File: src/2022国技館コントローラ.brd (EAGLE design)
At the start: 44 parts

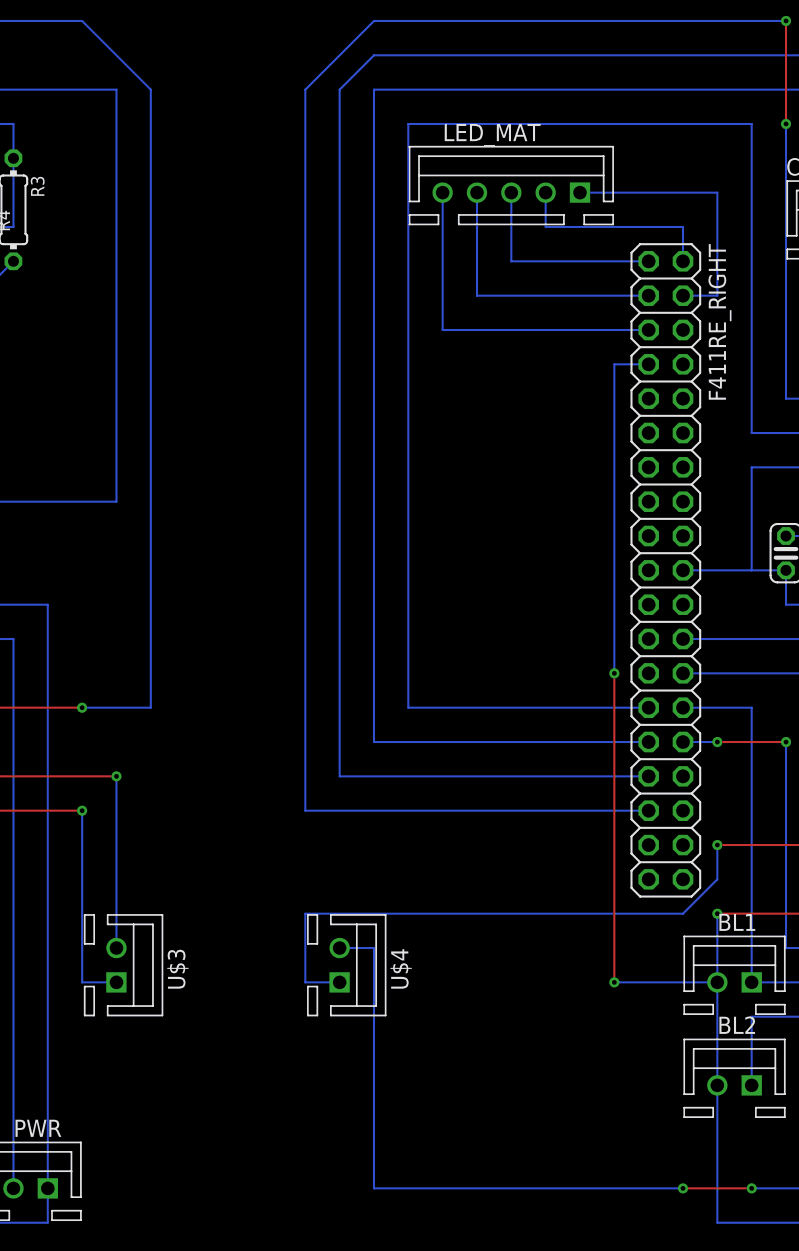
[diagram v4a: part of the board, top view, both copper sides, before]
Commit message: 足回りコントローラ
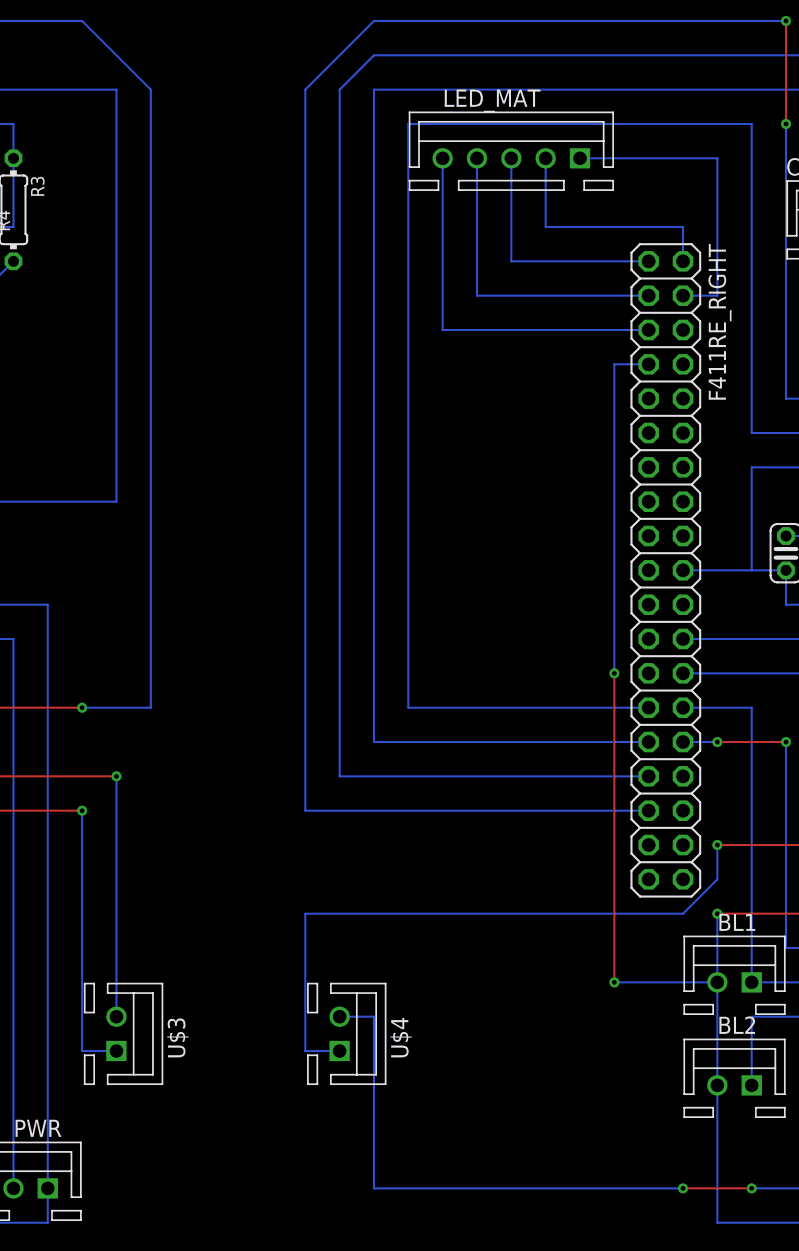
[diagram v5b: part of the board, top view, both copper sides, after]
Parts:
- moved U$3 5.08 mm to (57.1, 16.5)
- moved U$4 5.08 mm to (73.7, 16.5)
- moved LED_MAT 2.54 mm to (86.4, 81.3)
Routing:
- net U/D2: track 84.9 -> 95.0 mm
- net LED5: track 20.3 -> 22.9 mm
- net LED4: track 15.2 -> 17.8 mm
- net LED3: track 15.2 -> 17.8 mm
- net LED2: track 20.3 -> 22.9 mm
- net LED1: track 25.4 -> 27.9 mm
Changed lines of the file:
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@@
 <attribute name="VALUE" x="29.21" y="21.59" size="1.778" layer="27" ratio="10"/>
 </element>
-<element name="LED_MAT" library="con-jst-xh (1)" package="B5B-XH" value="" x="86.36" y="78.74" smashed="yes">
-<attribute name="NAME" x="81.28" y="82.55" size="1.27" layer="25"/>
-<attribute name="VALUE" x="81.28" y="74.93" size="1.27" layer="27"/>
+<element name="LED_MAT" library="con-jst-xh (1)" package="B5B-XH" value="" x="86.36" y="81.28" smashed="yes">
+<attribute name="NAME" x="81.28" y="85.09" size="1.27" layer="25"/>
+<attribute name="VALUE" x="81.28" y="77.47" size="1.27" layer="27"/>
 </element>
 <element name="C3" library="rcl" library_urn="urn:adsk.eagle:library:334" package="C025-024X044" package3d_urn="urn:adsk.eagle:package:23630/1" value="100nF" x="41.91" y="44.45" smashed="yes" rot="MR270">
@@
 <attribute name="VALUE" x="44.577" y="46.228" size="1.27" layer="28" ratio="10" rot="MR270"/>
 </element>
-<element name="U$3" library="con-jst-xh (1)" package="B2B-XH" value="02-JST" x="57.15" y="21.59" smashed="yes" rot="R270">
-<attribute name="NAME" x="60.96" y="22.86" size="1.27" layer="25" rot="R270"/>
-<attribute name="VALUE" x="53.34" y="22.86" size="1.27" layer="27" rot="R270"/>
+<element name="U$3" library="con-jst-xh (1)" package="B2B-XH" value="02-JST" x="57.15" y="16.51" smashed="yes" rot="R270">
+<attribute name="NAME" x="60.96" y="17.78" size="1.27" layer="25" rot="R270"/>
+<attribute name="VALUE" x="53.34" y="17.78" size="1.27" layer="27" rot="R270"/>
 </element>
-<element name="U$4" library="con-jst-xh (1)" package="B2B-XH" value="02-JST" x="73.66" y="21.59" smashed="yes" rot="R270">
-<attribute name="NAME" x="77.47" y="22.86" size="1.27" layer="25" rot="R270"/>
-<attribute name="VALUE" x="69.85" y="22.86" size="1.27" layer="27" rot="R270"/>
+<element name="U$4" library="con-jst-xh (1)" package="B2B-XH" value="02-JST" x="73.66" y="16.51" smashed="yes" rot="R270">
+<attribute name="NAME" x="77.47" y="17.78" size="1.27" layer="25" rot="R270"/>
+<attribute name="VALUE" x="69.85" y="17.78" size="1.27" layer="27" rot="R270"/>
 </element>
 </elements>
@@
 <contactref element="U$4" pad="2"/>
 <wire x1="36.83" y1="35.56" x2="41.91" y2="35.56" width="0.1524" layer="16"/>
-<wire x1="57.15" y1="22.86" x2="57.15" y2="35.56" width="0.1524" layer="16"/>
+<wire x1="57.15" y1="17.78" x2="57.15" y2="35.56" width="0.1524" layer="16"/>
 <via x="41.91" y="35.56" extent="1-16" drill="0.35"/>
 <via x="57.15" y="35.56" extent="1-16" drill="0.35"/>
@@
 <wire x1="134.62" y1="7.62" x2="132.08" y2="5.08" width="0.1524" layer="16"/>
 <wire x1="132.08" y1="5.08" x2="104.14" y2="5.08" width="0.1524" layer="16"/>
-<wire x1="73.66" y1="22.86" x2="76.2" y2="22.86" width="0.1524" layer="16"/>
-<wire x1="76.2" y1="22.86" x2="76.2" y2="5.08" width="0.1524" layer="16"/>
+<wire x1="73.66" y1="17.78" x2="76.2" y2="17.78" width="0.1524" layer="16"/>
+<wire x1="76.2" y1="17.78" x2="76.2" y2="5.08" width="0.1524" layer="16"/>
 <wire x1="76.2" y1="5.08" x2="99.06" y2="5.08" width="0.1524" layer="16"/>
 <via x="104.14" y="5.08" extent="1-16" drill="0.35"/>
 <via x="99.06" y="5.08" extent="1-16" drill="0.35"/>
 <wire x1="104.14" y1="5.08" x2="99.06" y2="5.08" width="0.1524" layer="1"/>
-<wire x1="57.15" y1="22.86" x2="73.66" y2="22.86" width="0" layer="19" extent="1-1"/>
+<wire x1="57.15" y1="17.78" x2="73.66" y2="17.78" width="0" layer="19" extent="1-1"/>
 </signal>
 <signal name="U/D2">
@@
 <contactref element="U$4" pad="1"/>
 <wire x1="36.83" y1="33.02" x2="41.91" y2="33.02" width="0.1524" layer="16"/>
-<wire x1="57.15" y1="20.32" x2="54.61" y2="20.32" width="0.1524" layer="16"/>
-<wire x1="54.61" y1="20.32" x2="54.61" y2="33.02" width="0.1524" layer="16"/>
+<wire x1="57.15" y1="15.24" x2="54.61" y2="15.24" width="0.1524" layer="16"/>
+<wire x1="54.61" y1="15.24" x2="54.61" y2="33.02" width="0.1524" layer="16"/>
 <via x="54.61" y="33.02" extent="1-16" drill="0.35"/>
 <via x="41.91" y="33.02" extent="1-16" drill="0.35"/>
 <wire x1="54.61" y1="33.02" x2="41.91" y2="33.02" width="0.1524" layer="1"/>
-<wire x1="73.66" y1="20.32" x2="71.12" y2="20.32" width="0.1524" layer="16"/>
-<wire x1="71.12" y1="20.32" x2="71.12" y2="25.4" width="0.1524" layer="16"/>
+<wire x1="73.66" y1="15.24" x2="71.12" y2="15.24" width="0.1524" layer="16"/>
+<wire x1="71.12" y1="15.24" x2="71.12" y2="25.4" width="0.1524" layer="16"/>
 <wire x1="71.12" y1="25.4" x2="99.06" y2="25.4" width="0.1524" layer="16"/>
 <wire x1="99.06" y1="25.4" x2="101.6" y2="27.94" width="0.1524" layer="16"/>
@@
 <via x="101.6" y="30.48" extent="1-16" drill="0.35"/>
 <wire x1="101.6" y1="30.48" x2="109.22" y2="30.48" width="0.1524" layer="1"/>
-<wire x1="57.15" y1="20.32" x2="73.66" y2="20.32" width="0" layer="19" extent="1-1"/>
+<wire x1="57.15" y1="15.24" x2="73.66" y2="15.24" width="0" layer="19" extent="1-1"/>
 </signal>
 <signal name="CK1_LEFT">
@@
 <contactref element="LED_MAT" pad="5"/>
 <contactref element="F411RE_RIGHT" pad="5"/>
-<wire x1="81.28" y1="78.74" x2="81.28" y2="68.58" width="0.1524" layer="16"/>
+<wire x1="81.28" y1="81.28" x2="81.28" y2="68.58" width="0.1524" layer="16"/>
 <wire x1="81.28" y1="68.58" x2="96.52" y2="68.58" width="0.1524" layer="16"/>
 </signal>
@@
 <contactref element="F411RE_RIGHT" pad="3"/>
 <contactref element="LED_MAT" pad="4"/>
-<wire x1="83.82" y1="78.74" x2="83.82" y2="71.12" width="0.1524" layer="16"/>
+<wire x1="83.82" y1="81.28" x2="83.82" y2="71.12" width="0.1524" layer="16"/>
 <wire x1="83.82" y1="71.12" x2="96.52" y2="71.12" width="0.1524" layer="16"/>
 </signal>
@@
 <contactref element="LED_MAT" pad="3"/>
 <contactref element="F411RE_RIGHT" pad="1"/>
-<wire x1="86.36" y1="78.74" x2="86.36" y2="73.66" width="0.1524" layer="16"/>
+<wire x1="86.36" y1="81.28" x2="86.36" y2="73.66" width="0.1524" layer="16"/>
 <wire x1="86.36" y1="73.66" x2="96.52" y2="73.66" width="0.1524" layer="16"/>
 </signal>
@@
 <contactref element="LED_MAT" pad="2"/>
 <wire x1="88.9" y1="76.2" x2="99.06" y2="76.2" width="0.1524" layer="16"/>
-<wire x1="88.9" y1="78.74" x2="88.9" y2="76.2" width="0.1524" layer="16"/>
+<wire x1="88.9" y1="81.28" x2="88.9" y2="76.2" width="0.1524" layer="16"/>
 <wire x1="99.06" y1="76.2" x2="99.06" y2="73.66" width="0.1524" layer="16"/>
 </signal>
@@
 <contactref element="LED_MAT" pad="1"/>
 <wire x1="99.06" y1="71.12" x2="101.6" y2="71.12" width="0.1524" layer="16"/>
-<wire x1="101.6" y1="78.74" x2="91.44" y2="78.74" width="0.1524" layer="16"/>
-<wire x1="101.6" y1="71.12" x2="101.6" y2="78.74" width="0.1524" layer="16"/>
+<wire x1="101.6" y1="81.28" x2="91.44" y2="81.28" width="0.1524" layer="16"/>
+<wire x1="101.6" y1="71.12" x2="101.6" y2="81.28" width="0.1524" layer="16"/>
 </signal>
 <signal name="BUSY">

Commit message: 国技館足回り修正前
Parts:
- removed LED_MAT: (no value), con-jst-xh (1):B5B-XH
- added EMERGENCY: (no value), con-jst-xh:B3B-XH
- added LED: (no value), con-jst-xh:B6B-XH
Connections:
- new net EME_SW: EMERGENCY.2, F411RE_LEFT.13
- net 3V3: now also EMERGENCY.3
- net GND: now also EMERGENCY.1, LED.1
- net LED1: now also LED.6; no longer LED_MAT.5
- net LED2: now also LED.5; no longer LED_MAT.4
- net LED3: now also LED.4; no longer LED_MAT.3
- net LED4: now also LED.3; no longer LED_MAT.2
- net LED5: now also LED.2; no longer LED_MAT.1
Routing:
- net EME_SW: track 0.00 -> 66.0 mm, vias 0 -> 2
- net GND: track 458.4 -> 520.4 mm, vias 0 -> 4
- net LED5: track 22.9 -> 25.4 mm
- net LED4: track 17.8 -> 15.2 mm
- net LED3: track 17.8 -> 15.2 mm
- net LED2: track 22.9 -> 20.3 mm
- net LED1: track 27.9 -> 25.4 mm
- net 3V3: track 576.1 -> 578.7 mm
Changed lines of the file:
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@@
 <attribute name="VALUE" x="29.21" y="21.59" size="1.778" layer="27" ratio="10"/>
-</element>
-<element name="LED_MAT" library="con-jst-xh (1)" package="B5B-XH" value="" x="86.36" y="81.28" smashed="yes">
-<attribute name="NAME" x="81.28" y="85.09" size="1.27" layer="25"/>
-<attribute name="VALUE" x="81.28" y="77.47" size="1.27" layer="27"/>
 </element>
 <element name="C3" library="rcl" library_urn="urn:adsk.eagle:library:334" package="C025-024X044" package3d_urn="urn:adsk.eagle:package:23630/1" value="100nF" x="41.91" y="44.45" smashed="yes" rot="MR270">
@@
 <attribute name="NAME" x="77.47" y="17.78" size="1.27" layer="25" rot="R270"/>
 <attribute name="VALUE" x="69.85" y="17.78" size="1.27" layer="27" rot="R270"/>
+</element>
+<element name="LED" library="con-jst-xh" package="B6B-XH" value="" x="87.63" y="78.74" smashed="yes">
+<attribute name="NAME" x="81.28" y="82.55" size="1.27" layer="25"/>
+<attribute name="VALUE" x="81.28" y="74.93" size="1.27" layer="27"/>
+</element>
+<element name="EMERGENCY" library="con-jst-xh" package="B3B-XH" value="" x="11.43" y="15.24" smashed="yes" rot="R180">
+<attribute name="NAME" x="16.51" y="11.43" size="1.27" layer="25" rot="R180"/>
+<attribute name="VALUE" x="13.97" y="19.05" size="1.27" layer="27" rot="R180"/>
 </element>
 </elements>
@@
 <contactref element="SV1" pad="3"/>
 <wire x1="26.67" y1="15.24" x2="26.67" y2="12.7" width="0.1524" layer="16"/>
-<wire x1="26.67" y1="12.7" x2="6.35" y2="12.7" width="0.1524" layer="16"/>
+<wire x1="26.67" y1="12.7" x2="13.97" y2="12.7" width="0.1524" layer="16"/>
+<wire x1="13.97" y1="12.7" x2="6.35" y2="12.7" width="0.1524" layer="16"/>
 <wire x1="6.35" y1="12.7" x2="6.35" y2="53.34" width="0.1524" layer="16"/>
 <wire x1="119.38" y1="20.32" x2="119.38" y2="25.4" width="0.1524" layer="16"/>
@@
 <via x="93.98" y="43.18" extent="1-16" drill="0.35"/>
 <wire x1="93.98" y1="43.18" x2="93.98" y2="20.32" width="0.1524" layer="1"/>
+<contactref element="EMERGENCY" pad="3"/>
+<wire x1="13.97" y1="15.24" x2="13.97" y2="12.7" width="0.1524" layer="16"/>
 <wire x1="36.83" y1="55.88" x2="93.98" y2="43.18" width="0" layer="19" extent="1-1"/>
 </signal>
@@
 <contactref element="F411RE_RIGHT" pad="20"/>
 <wire x1="106.68" y1="50.8" x2="104.14" y2="50.8" width="0.1524" layer="16"/>
-<wire x1="104.14" y1="50.8" x2="99.06" y2="50.8" width="0.1524" layer="16"/>
+<wire x1="104.14" y1="50.8" x2="101.6" y2="50.8" width="0.1524" layer="16"/>
+<wire x1="101.6" y1="50.8" x2="99.06" y2="50.8" width="0.1524" layer="16"/>
 <wire x1="106.68" y1="50.8" x2="106.68" y2="48.26" width="0.1524" layer="16"/>
 <wire x1="132.08" y1="12.7" x2="129.54" y2="12.7" width="0.1524" layer="16"/>
@@
 <wire x1="106.68" y1="48.26" x2="129.54" y2="48.26" width="0.1524" layer="16"/>
 <wire x1="129.54" y1="48.26" x2="129.54" y2="22.86" width="0.1524" layer="16"/>
-<wire x1="49.53" y1="73.66" x2="99.06" y2="50.8" width="0" layer="19" extent="1-1"/>
+<contactref element="LED" pad="1"/>
+<wire x1="93.98" y1="78.74" x2="99.06" y2="78.74" width="0.1524" layer="16"/>
+<via x="99.06" y="78.74" extent="1-16" drill="0.35"/>
+<wire x1="99.06" y1="78.74" x2="101.6" y2="76.2" width="0.1524" layer="1"/>
+<wire x1="101.6" y1="76.2" x2="101.6" y2="53.34" width="0.1524" layer="1"/>
+<via x="101.6" y="53.34" extent="1-16" drill="0.35"/>
+<wire x1="101.6" y1="53.34" x2="101.6" y2="50.8" width="0.1524" layer="16"/>
+<contactref element="EMERGENCY" pad="1"/>
+<wire x1="8.89" y1="15.24" x2="8.89" y2="20.32" width="0.1524" layer="16"/>
+<via x="8.89" y="20.32" extent="1-16" drill="0.35"/>
+<wire x1="8.89" y1="20.32" x2="-6.35" y2="20.32" width="0.1524" layer="1"/>
+<via x="-6.35" y="20.32" extent="1-16" drill="0.35"/>
+<wire x1="-6.35" y1="20.32" x2="-6.35" y2="27.94" width="0.1524" layer="16"/>
+<wire x1="49.53" y1="73.66" x2="93.98" y2="78.74" width="0" layer="19" extent="1-1"/>
 <wire x1="34.29" y1="50.8" x2="36.83" y2="66.04" width="0" layer="19" extent="1-1"/>
 <wire x1="36.83" y1="48.26" x2="34.29" y2="50.8" width="0" layer="19" extent="1-1"/>
@@
 <wire x1="24.13" y1="68.58" x2="11.43" y2="68.58" width="0.1524" layer="16"/>
 <wire x1="41.91" y1="73.66" x2="36.83" y2="73.66" width="0.1524" layer="16"/>
-<wire x1="36.83" y1="73.66" x2="41.91" y2="73.66" width="0" layer="19"/>
 </signal>
 <signal name="CK2_UP">
@@
 </signal>
 <signal name="LED1">
-<contactref element="LED_MAT" pad="5"/>
 <contactref element="F411RE_RIGHT" pad="5"/>
-<wire x1="81.28" y1="81.28" x2="81.28" y2="68.58" width="0.1524" layer="16"/>
-<wire x1="81.28" y1="68.58" x2="96.52" y2="68.58" width="0.1524" layer="16"/>
+<wire x1="96.52" y1="68.58" x2="81.28" y2="68.58" width="0.1524" layer="16"/>
+<contactref element="LED" pad="6"/>
+<wire x1="81.28" y1="68.58" x2="81.28" y2="78.74" width="0.1524" layer="16"/>
 </signal>
 <signal name="LED2">
 <contactref element="F411RE_RIGHT" pad="3"/>
-<contactref element="LED_MAT" pad="4"/>
-<wire x1="83.82" y1="81.28" x2="83.82" y2="71.12" width="0.1524" layer="16"/>
-<wire x1="83.82" y1="71.12" x2="96.52" y2="71.12" width="0.1524" layer="16"/>
+<wire x1="96.52" y1="71.12" x2="83.82" y2="71.12" width="0.1524" layer="16"/>
+<contactref element="LED" pad="5"/>
+<wire x1="83.82" y1="71.12" x2="83.82" y2="78.74" width="0.1524" layer="16"/>
 </signal>
 <signal name="LED3">
-<contactref element="LED_MAT" pad="3"/>
 <contactref element="F411RE_RIGHT" pad="1"/>
-<wire x1="86.36" y1="81.28" x2="86.36" y2="73.66" width="0.1524" layer="16"/>
-<wire x1="86.36" y1="73.66" x2="96.52" y2="73.66" width="0.1524" layer="16"/>
+<wire x1="96.52" y1="73.66" x2="86.36" y2="73.66" width="0.1524" layer="16"/>
+<contactref element="LED" pad="4"/>
+<wire x1="86.36" y1="73.66" x2="86.36" y2="78.74" width="0.1524" layer="16"/>
 </signal>
 <signal name="LED4">
 <contactref element="F411RE_RIGHT" pad="2"/>
-<contactref element="LED_MAT" pad="2"/>
-<wire x1="88.9" y1="76.2" x2="99.06" y2="76.2" width="0.1524" layer="16"/>
-<wire x1="88.9" y1="81.28" x2="88.9" y2="76.2" width="0.1524" layer="16"/>
+<wire x1="99.06" y1="76.2" x2="88.9" y2="76.2" width="0.1524" layer="16"/>
 <wire x1="99.06" y1="76.2" x2="99.06" y2="73.66" width="0.1524" layer="16"/>
+<contactref element="LED" pad="3"/>
+<wire x1="88.9" y1="76.2" x2="88.9" y2="78.74" width="0.1524" layer="16"/>
 </signal>
 <signal name="LED5">
 <contactref element="F411RE_RIGHT" pad="4"/>
-<contactref element="LED_MAT" pad="1"/>
 <wire x1="99.06" y1="71.12" x2="101.6" y2="71.12" width="0.1524" layer="16"/>
+<wire x1="101.6" y1="71.12" x2="101.6" y2="81.28" width="0.1524" layer="16"/>
+<contactref element="LED" pad="2"/>
 <wire x1="101.6" y1="81.28" x2="91.44" y2="81.28" width="0.1524" layer="16"/>
-<wire x1="101.6" y1="71.12" x2="101.6" y2="81.28" width="0.1524" layer="16"/>
+<wire x1="91.44" y1="81.28" x2="91.44" y2="78.74" width="0.1524" layer="16"/>
 </signal>
 <signal name="BUSY">
@@
 <wire x1="49.53" y1="45.72" x2="41.91" y2="45.72" width="0.1524" layer="16"/>
 </signal>
+<signal name="EME_SW">
+<contactref element="F411RE_LEFT" pad="13"/>
+<contactref element="EMERGENCY" pad="2"/>
+<wire x1="11.43" y1="15.24" x2="11.43" y2="50.8" width="0.1524" layer="16"/>
+<via x="11.43" y="50.8" extent="1-16" drill="0.35"/>
+<wire x1="11.43" y1="50.8" x2="11.43" y2="58.42" width="0.1524" layer="1"/>
+<via x="11.43" y="58.42" extent="1-16" drill="0.35"/>
+<wire x1="11.43" y1="58.42" x2="34.29" y2="58.42" width="0.1524" layer="16"/>
+</signal>
 </signals>
